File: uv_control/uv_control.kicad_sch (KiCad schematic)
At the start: 20 parts, among them J1 Safety, J2 Fan, J3 12V Power, J4 Light Power, Q1 BSS138, Q2 BSS138, Q3 IRFS7730-7, U1 L7805, U2 MCP1415

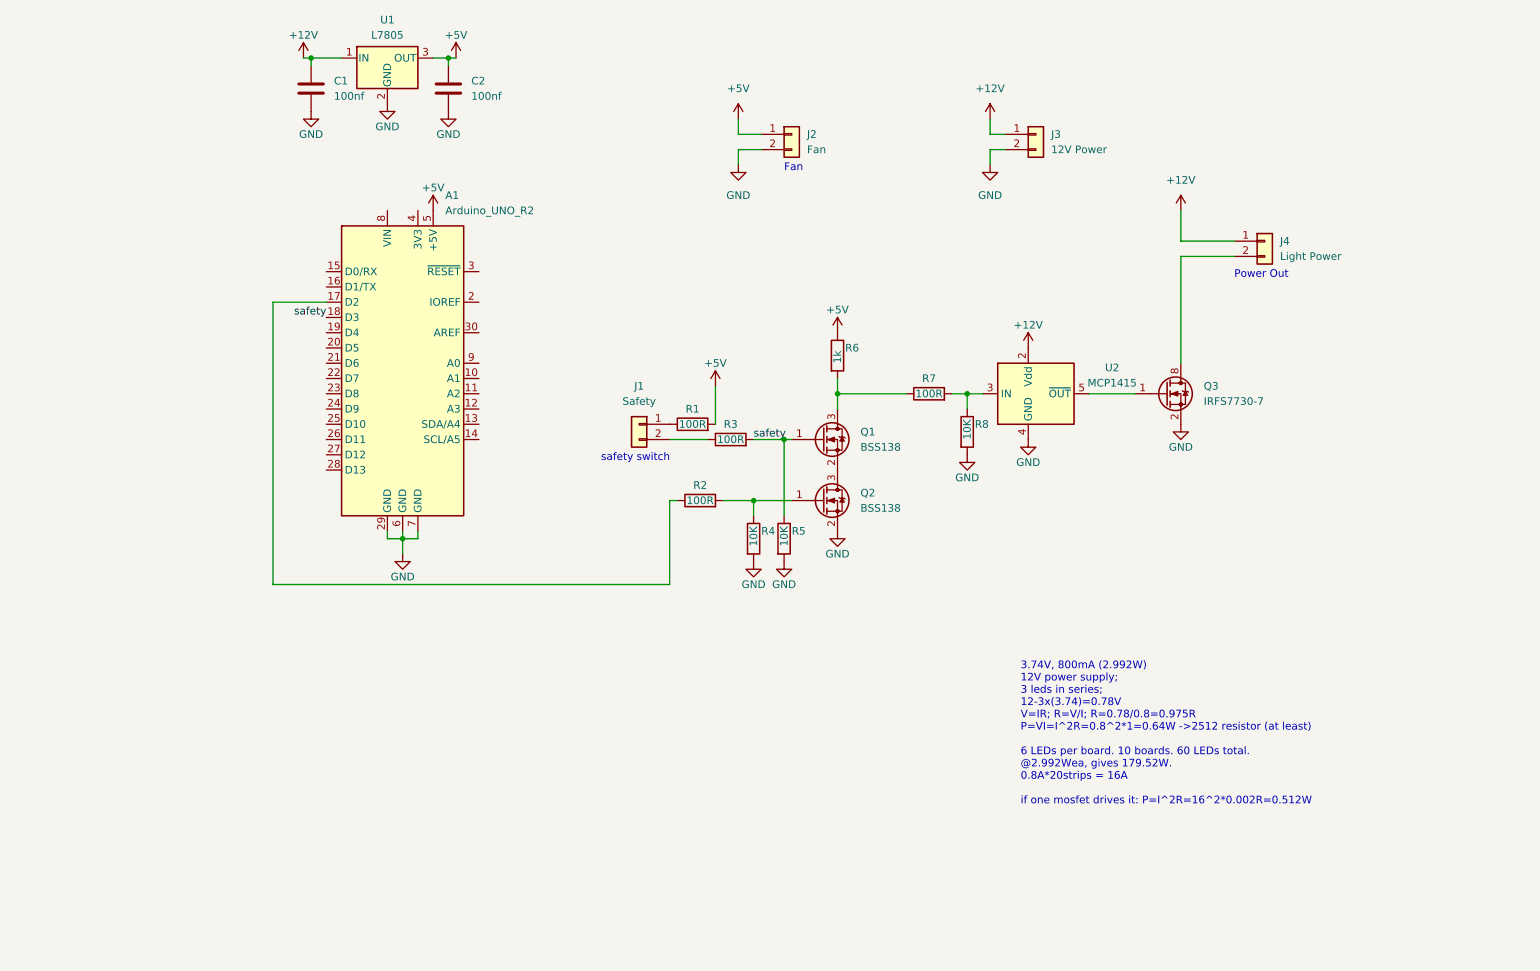
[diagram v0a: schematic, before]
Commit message: Updating control board to include more pinouts
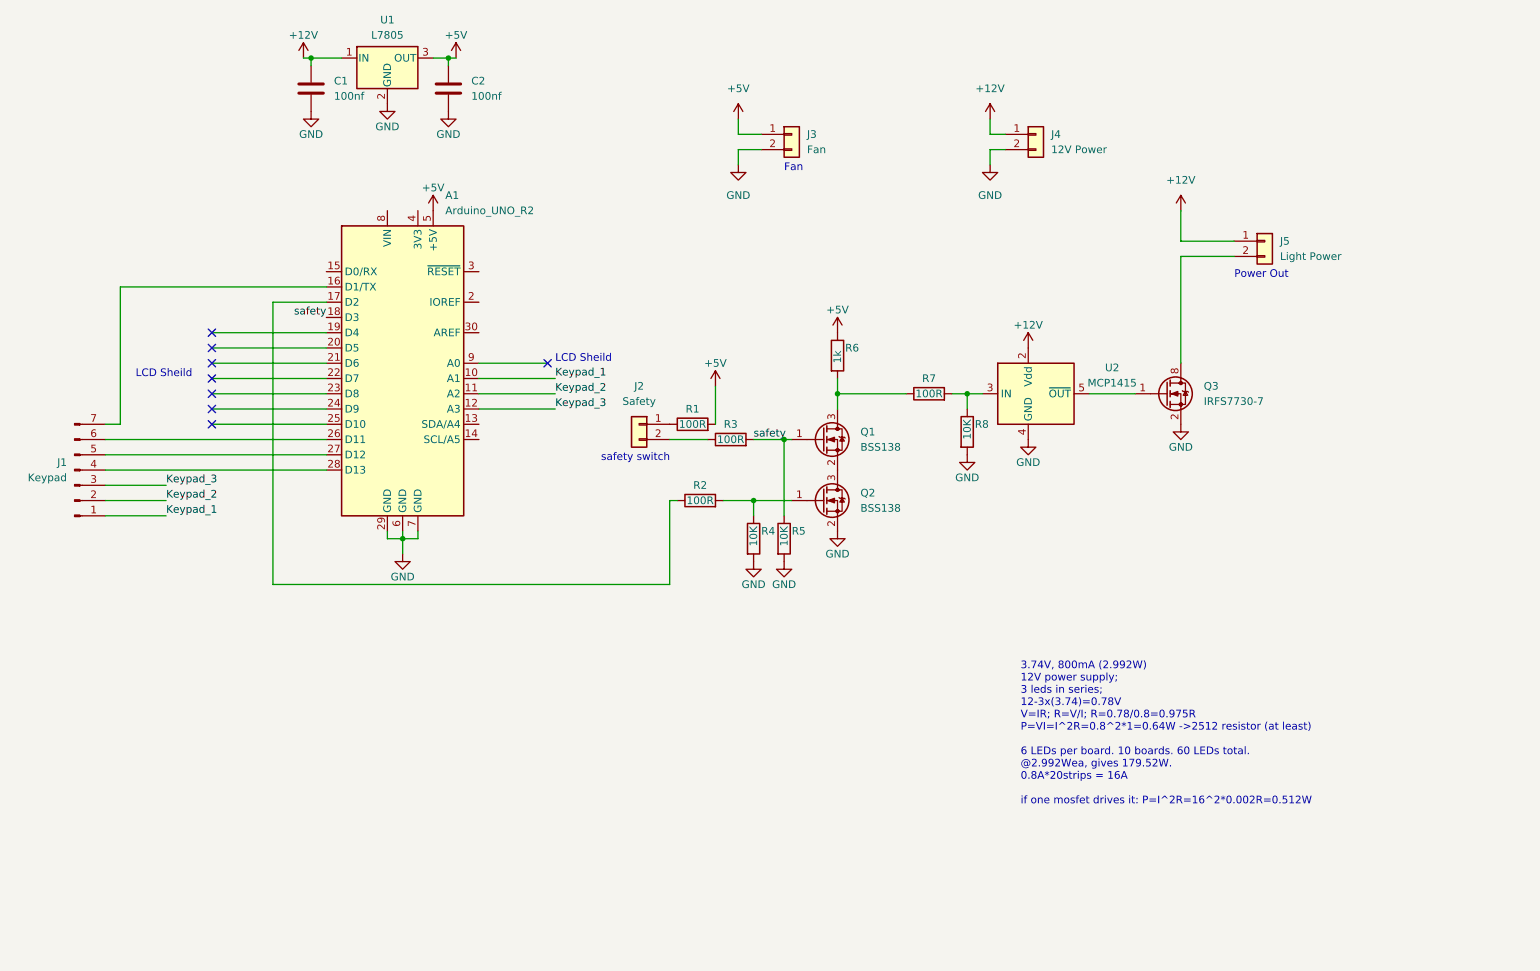
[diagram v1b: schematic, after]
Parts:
- added J1: Keypad, Connector_JST:JST_EH_B7B-EH-A_1x07_P2.50mm_Vertical, symbol Connector:Conn_01x07_Male
- renumbered J1 to J2, J2 to J3, J3 to J4, J4 to J5
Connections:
- net Keypad_1: now reaches A1.10 (A1)
- net Keypad_1: now also J1.1 (Pin_1)
- net Keypad_2: now reaches A1.11 (A2)
- net Keypad_2: now also J1.2 (Pin_2)
- net Keypad_3: now reaches A1.12 (A3)
- net Keypad_3: now also J1.3 (Pin_3)
- net at A1.16 (D1/TX): now also J1.7 (Pin_7)
- net at A1.26 (D11): now also J1.6 (Pin_6)
- net at A1.27 (D12): now also J1.5 (Pin_5)
- net at A1.28 (D13): now also J1.4 (Pin_4)
- no-connect marks 0 -> 8
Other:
- note added: "LCD Sheild"

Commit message: Updated wiring to avoid Serial debug port
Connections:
- net at A1.16 (D1/TX): no longer J1.7 (Pin_7)
- net Keypad_4: now reaches A1.13 (SDA/A4)
- net Keypad_4: now also J1.7 (Pin_7)
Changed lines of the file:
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@@
+    (stroke (width 0) (type default) (color 0 0 0 0))
+  )
+  (wire (pts (xy 95.25 86.36) (xy 107.95 86.36))
     (stroke (width 0) (type default) (color 0 0 0 0))
   )
@@
     (stroke (width 0) (type default) (color 0 0 0 0))
   )
-  (wire (pts (xy 35.56 63.5) (xy 69.85 63.5))
-    (stroke (width 0) (type default) (color 0 0 0 0))
-  )
   (wire (pts (xy 154.94 81.28) (xy 166.37 81.28))
     (stroke (width 0) (type default) (color 0 0 0 0))
@@
   )
   (wire (pts (xy 50.8 78.74) (xy 69.85 78.74))
-    (stroke (width 0) (type default) (color 0 0 0 0))
-  )
-  (wire (pts (xy 35.56 63.5) (xy 35.56 86.36))
     (stroke (width 0) (type default) (color 0 0 0 0))
   )
@@
     (effects (font (size 1.27 1.27)) (justify left bottom))
   )
+  (label "Keypad_4" (at 107.95 86.36 0)
+    (effects (font (size 1.27 1.27)) (justify left bottom))
+  )
   (label "Keypad_3" (at 107.95 83.82 0)
     (effects (font (size 1.27 1.27)) (justify left bottom))
@@
     (effects (font (size 1.27 1.27)) (justify left bottom))
   )
+  (label "Keypad_4" (at 35.56 86.36 0)
+    (effects (font (size 1.27 1.27)) (justify left bottom))
+  )

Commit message: Updating pinout
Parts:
- added D1: LED, symbol Device:LED
- added R1: 220, symbol Device:R
- renumbered R1 to R2, R2 to R3, R3 to R4, R4 to R5, R5 to R6, R6 to R7, R7 to R8, R8 to R9
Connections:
- net GND: now also D1.1 (K)
- net at A1.14 (SCL/A5): now also R1.1
- new net: D1.2 (A), R1.2
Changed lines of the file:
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@@
   (junction (at 67.31 25.4) (diameter 0) (color 0 0 0 0)
+  )
+  (junction (at 85.09 105.41) (diameter 0) (color 0 0 0 0)
   )
   (junction (at 146.05 88.9) (diameter 0) (color 0 0 0 0)
@@
     (stroke (width 0) (type default) (color 0 0 0 0))
   )
+  (wire (pts (xy 95.25 88.9) (xy 101.6 88.9))
+    (stroke (width 0) (type default) (color 0 0 0 0))
+  )
   (wire (pts (xy 80.01 105.41) (xy 82.55 105.41))
     (stroke (width 0) (type default) (color 0 0 0 0))
@@
     (stroke (width 0) (type default) (color 0 0 0 0))
   )
+  (wire (pts (xy 101.6 96.52) (xy 101.6 97.79))
+    (stroke (width 0) (type default) (color 0 0 0 0))
+  )
   (wire (pts (xy 180.34 43.18) (xy 180.34 40.64))
     (stroke (width 0) (type default) (color 0 0 0 0))
   )
+  (wire (pts (xy 85.09 105.41) (xy 101.6 105.41))
+    (stroke (width 0) (type default) (color 0 0 0 0))
+  )
   (wire (pts (xy 50.8 76.2) (xy 69.85 76.2))
     (stroke (width 0) (type default) (color 0 0 0 0))
@@
     (stroke (width 0) (type default) (color 0 0 0 0))
   )
-  (wire (pts (xy 85.09 105.41) (xy 82.55 105.41))
+  (wire (pts (xy 82.55 105.41) (xy 85.09 105.41))
     (stroke (width 0) (type default) (color 0 0 0 0))
   )
@@
     (effects (font (size 1.27 1.27)) (justify left bottom))
   )
+  (symbol (lib_id "Device:LED") (at 101.6 101.6 90) (unit 1)
+    (in_bom yes) (on_board yes) (fields_autoplaced)
+    (property "Reference" "D1" (id 0) (at 105.41 101.9174 90)
+      (effects (font (size 1.27 1.27)) (justify right))
+    )
+    (property "Value" "LED" (id 1) (at 105.41 104.4574 90)
+      (effects (font (size 1.27 1.27)) (justify right))
+    )
+    (property "Footprint" "" (id 2) (at 101.6 101.6 0)
+      (effects (font (size 1.27 1.27)) hide)
+    )
+    (property "Datasheet" "~" (id 3) (at 101.6 101.6 0)
+      (effects (font (size 1.27 1.27)) hide)
+    )
+    (pin "1")
+    (pin "2")
+  )
   (symbol (lib_id "Device:R") (at 170.18 81.28 90) (unit 1)
     (in_bom yes) (on_board yes)
-    (property "Reference" "R7" (id 0) (at 170.18 78.74 90))
+    (property "Reference" "R8" (id 0) (at 170.18 78.74 90))
     (property "Value" "100R" (id 1) (at 170.18 81.28 90))
     (property "Footprint" "Resistor_SMD:R_0805_2012Metric" (id 2) (at 170.18 83.058 90)
@@
     (pin "1")
   )
+  (symbol (lib_id "Device:R") (at 101.6 92.71 0) (unit 1)
+    (in_bom yes) (on_board yes) (fields_autoplaced)
+    (property "Reference" "R1" (id 0) (at 104.14 91.4399 0)
+      (effects (font (size 1.27 1.27)) (justify left))
+    )
+    (property "Value" "220" (id 1) (at 104.14 93.9799 0)
+      (effects (font (size 1.27 1.27)) (justify left))
+    )
+    (property "Footprint" "" (id 2) (at 99.822 92.71 90)
+      (effects (font (size 1.27 1.27)) hide)
+    )
+    (property "Datasheet" "~" (id 3) (at 101.6 92.71 0)
+      (effects (font (size 1.27 1.27)) hide)
+    )
+    (pin "1")
+    (pin "2")
+  )
   (symbol (lib_id "power:GND") (at 154.94 104.14 0) (unit 1)
     (in_bom yes) (on_board yes)
@@
   (symbol (lib_id "Device:R") (at 176.53 87.63 0) (unit 1)
     (in_bom yes) (on_board yes)
-    (property "Reference" "R8" (id 0) (at 177.8 86.36 0)
+    (property "Reference" "R9" (id 0) (at 177.8 86.36 0)
       (effects (font (size 1.27 1.27)) (justify left))
     )
@@
   (symbol (lib_id "Device:R") (at 140.97 105.41 0) (unit 1)
     (in_bom yes) (on_board yes)
-    (property "Reference" "R4" (id 0) (at 142.24 104.14 0)
+    (property "Reference" "R5" (id 0) (at 142.24 104.14 0)
       (effects (font (size 1.27 1.27)) (justify left))
     )
@@
   (symbol (lib_id "Device:R") (at 154.94 74.93 0) (unit 1)
     (in_bom yes) (on_board yes)
-    (property "Reference" "R6" (id 0) (at 156.21 73.66 0)
+    (property "Reference" "R7" (id 0) (at 156.21 73.66 0)
       (effects (font (size 1.27 1.27)) (justify left))
     )
@@
   (symbol (lib_id "Device:R") (at 146.05 105.41 0) (unit 1)
     (in_bom yes) (on_board yes)
-    (property "Reference" "R5" (id 0) (at 147.32 104.14 0)
+    (property "Reference" "R6" (id 0) (at 147.32 104.14 0)
       (effects (font (size 1.27 1.27)) (justify left))
     )
@@
   (symbol (lib_id "Device:R") (at 137.16 88.9 90) (unit 1)
     (in_bom yes) (on_board yes)
-    (property "Reference" "R3" (id 0) (at 137.16 86.36 90))
+    (property "Reference" "R4" (id 0) (at 137.16 86.36 90))
     (property "Value" "100R" (id 1) (at 137.16 88.9 90))
     (property "Footprint" "Resistor_SMD:R_0805_2012Metric" (id 2) (at 137.16 90.678 90)
@@
   (symbol (lib_id "Device:R") (at 130.81 86.36 90) (unit 1)
     (in_bom yes) (on_board yes)
-    (property "Reference" "R1" (id 0) (at 130.81 83.82 90))
+    (property "Reference" "R2" (id 0) (at 130.81 83.82 90))
     (property "Value" "100R" (id 1) (at 130.81 86.36 90))
     (property "Footprint" "Resistor_SMD:R_0805_2012Metric" (id 2) (at 130.81 88.138 90)
@@
   (symbol (lib_id "Device:R") (at 132.08 99.06 90) (unit 1)
     (in_bom yes) (on_board yes)
-    (property "Reference" "R2" (id 0) (at 132.08 96.52 90))
+    (property "Reference" "R3" (id 0) (at 132.08 96.52 90))
     (property "Value" "100R" (id 1) (at 132.08 99.06 90))
     (property "Footprint" "Resistor_SMD:R_0805_2012Metric" (id 2) (at 132.08 100.838 90)
@@
       (reference "C2") (unit 1) (value "100nf") (footprint "Capacitor_SMD:C_1206_3216Metric")
     )
+    (path "/0179f660-c3db-4b35-9015-787d5970b1bb"
+      (reference "D1") (unit 1) (value "LED") (footprint "")
+    )
     (path "/b928be8d-205b-4cd7-98e1-8918680f56aa"
       (reference "J1") (unit 1) (value "Keypad") (footprint "Connector_JST:JST_EH_B7B-EH-A_1x07_P2.50mm_Vertical")
@@
       (reference "Q3") (unit 1) (value "IRFS7730-7") (footprint "Package_TO_SOT_SMD:TO-263-7_TabPin8")
     )
+    (path "/2ace17d0-df02-4bb0-b8ca-79d4e4d58c80"
+      (reference "R1") (unit 1) (value "220") (footprint "")
+    )
     (path "/ceee8033-6fe8-4f4b-ae23-812eb071c1ea"
-      (reference "R1") (unit 1) (value "100R") (footprint "Resistor_SMD:R_0805_2012Metric")
+      (reference "R2") (unit 1) (value "100R") (footprint "Resistor_SMD:R_0805_2012Metric")
     )
     (path "/d13251bc-002b-40e1-8abe-53818983e59e"
-      (reference "R2") (unit 1) (value "100R") (footprint "Resistor_SMD:R_0805_2012Metric")
+      (reference "R3") (unit 1) (value "100R") (footprint "Resistor_SMD:R_0805_2012Metric")
     )
     (path "/c2e9dc06-dab4-4e31-a3ac-a894ffd9e76c"
-      (reference "R3") (unit 1) (value "100R") (footprint "Resistor_SMD:R_0805_2012Metric")
+      (reference "R4") (unit 1) (value "100R") (footprint "Resistor_SMD:R_0805_2012Metric")
     )
     (path "/79180556-ccf3-40e7-9ec8-f07ec71f3a9c"
-      (reference "R4") (unit 1) (value "10K") (footprint "Resistor_SMD:R_0805_2012Metric")
+      (reference "R5") (unit 1) (value "10K") (footprint "Resistor_SMD:R_0805_2012Metric")
     )
     (path "/858cdf00-2dcb-4654-97af-970a1c0e606c"
-      (reference "R5") (unit 1) (value "10K") (footprint "Resistor_SMD:R_0805_2012Metric")
+      (reference "R6") (unit 1) (value "10K") (footprint "Resistor_SMD:R_0805_2012Metric")
     )
     (path "/7fd0b62a-aabe-4bdd-a5df-8b800aa4bd30"
-      (reference "R6") (unit 1) (value "1k") (footprint "Resistor_SMD:R_0805_2012Metric")
+      (reference "R7") (unit 1) (value "1k") (footprint "Resistor_SMD:R_0805_2012Metric")
     )
     (path "/042da3e9-0c64-49c8-9cb2-7052e827efca"
-      (reference "R7") (unit 1) (value "100R") (footprint "Resistor_SMD:R_0805_2012Metric")
+      (reference "R8") (unit 1) (value "100R") (footprint "Resistor_SMD:R_0805_2012Metric")
     )
     (path "/3b4d448c-def5-4665-9b67-a2ffbc10d39f"
-      (reference "R8") (unit 1) (value "10K") (footprint "Resistor_SMD:R_0805_2012Metric")
+      (reference "R9") (unit 1) (value "10K") (footprint "Resistor_SMD:R_0805_2012Metric")
     )
     (path "/1b425e46-20fc-4aaf-a510-d3558dcf4d4b"
